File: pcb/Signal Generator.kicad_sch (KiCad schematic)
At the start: 3 parts, among them J2 AudioJack3, J3 Conn_02x02_Odd_Even, J4 Screw_Terminal_01x04

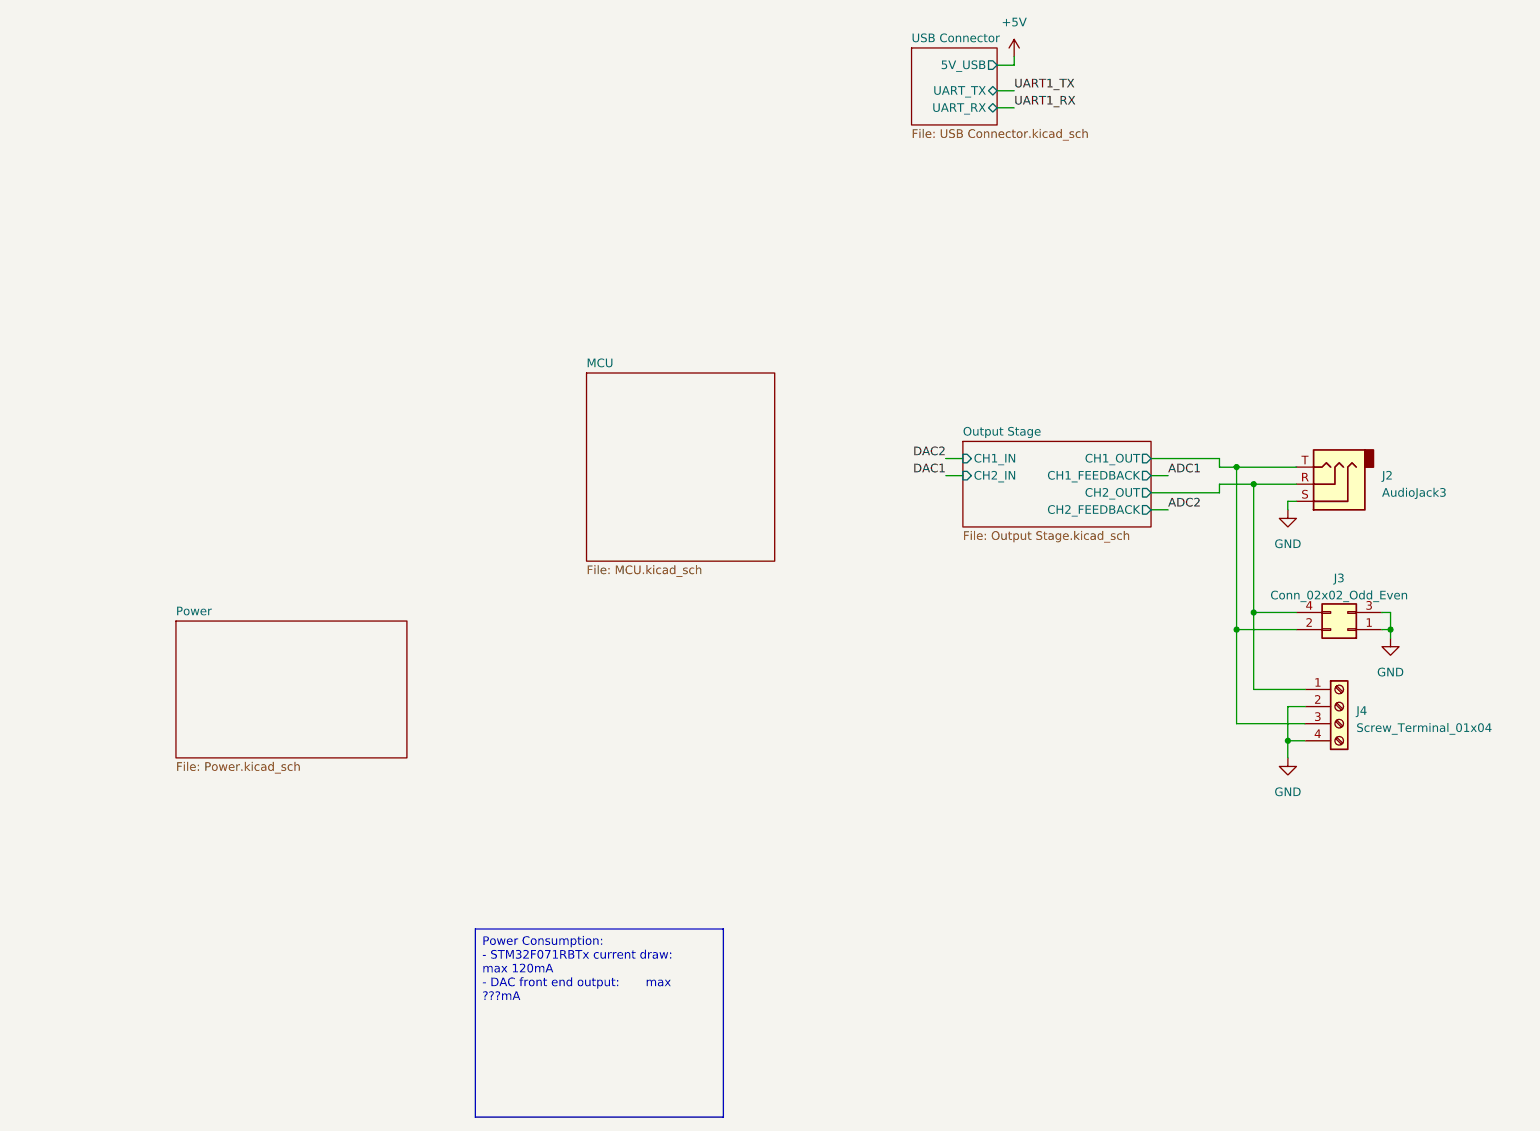
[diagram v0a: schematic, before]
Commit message: Completed schematic oranization and components connection
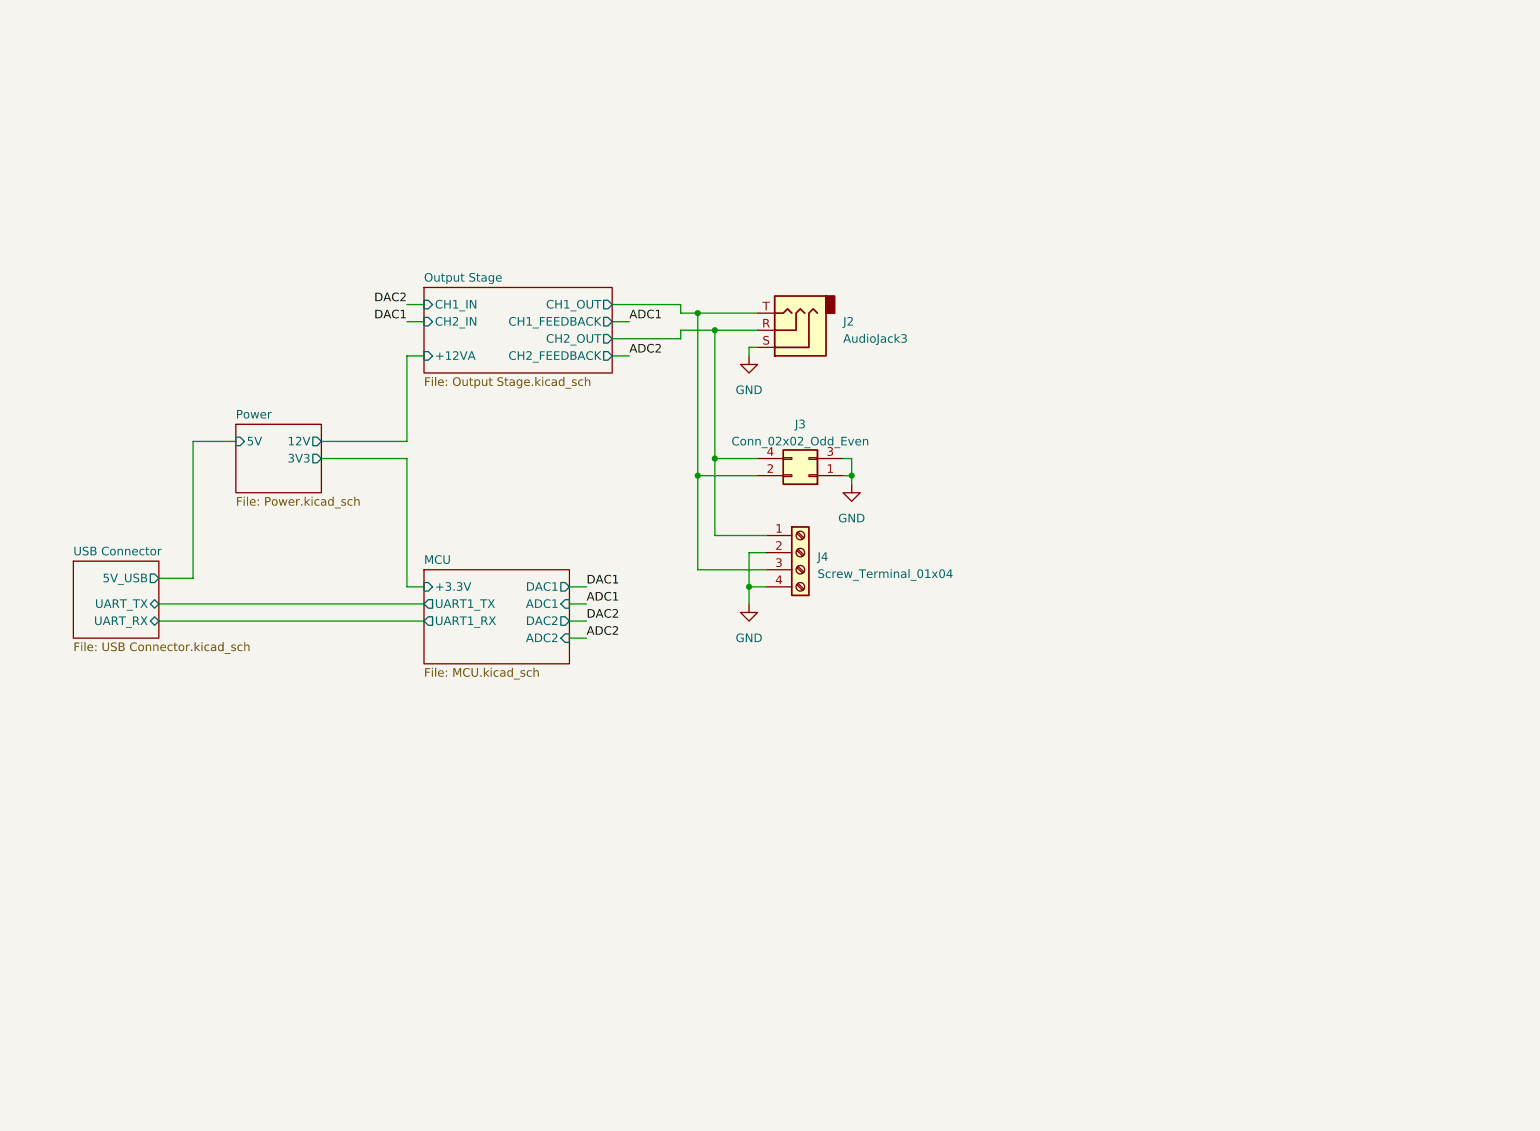
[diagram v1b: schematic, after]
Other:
- sheet MCU ports: added +3.3V, ADC1, ADC2, DAC1, DAC2, UART1_RX, UART1_TX; removed none
- sheet Output Stage ports: added +12VA; removed none
- sheet Power ports: added 12V, 3V3, 5V; removed none
- moved on the sheet: J2, J3, J4

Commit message: Added micro SD and RGB led to schematic. Also added components part numbers
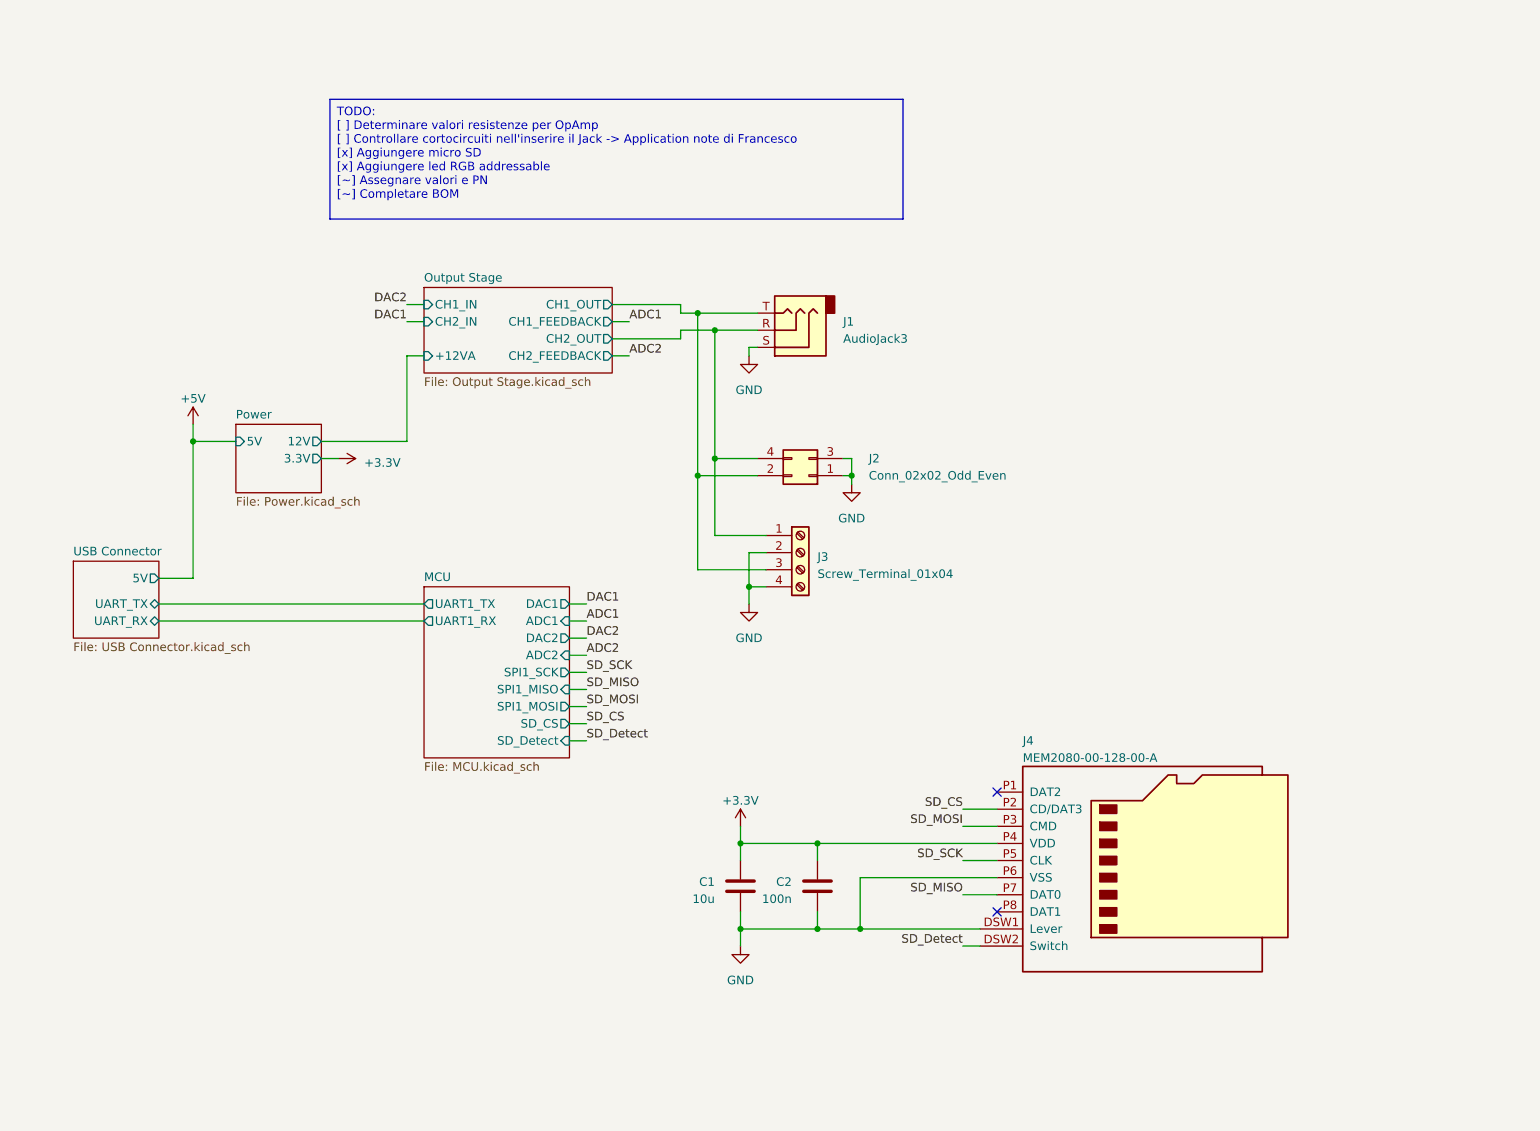
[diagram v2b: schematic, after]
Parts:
- added C1: 10u, Capacitor_SMD:C_0603_1608Metric, symbol Device:C
- added C2: 100n, Capacitor_SMD:C_0603_1608Metric, symbol Device:C
- added J4: MEM2080-00-128-00-A, Signal Generator Components:MEM2080-00-128-00-A, symbol Signal Generator Components:MEM2080-00-128-00-A
- J1: renamed from J2; PN (none) -> SJ-3523-SMT-TR
- J2: renamed from J3; PN (none) -> 10129382-904001BLF
- J3: renamed from J4; PN (none) -> 1725672
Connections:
- net GND: now also C1.2, C2.2, J4.DSW1 (Lever), J4.P6 (VSS)
- new net +3.3V: C1.1, C2.1, J4.P4 (VDD)
- new net SD_CS: J4.P2 (CD/DAT3)
- new net SD_Detect: J4.DSW2 (Switch)
- new net SD_MISO: J4.P7 (DAT0)
- new net SD_MOSI: J4.P3 (CMD)
- new net SD_SCK: J4.P5 (CLK)
- no-connect marks 0 -> 2
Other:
- sheet MCU ports: added SD_CS, SD_Detect, SPI1_MISO, SPI1_MOSI, SPI1_SCK; removed +3.3V
- sheet Power ports: added 3.3V; removed 3V3
- sheet USB Connector ports: added 5V; removed 5V_USB

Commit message: Completed schematic and tried some simulations
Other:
- moved on the sheet: J1, J2, J3

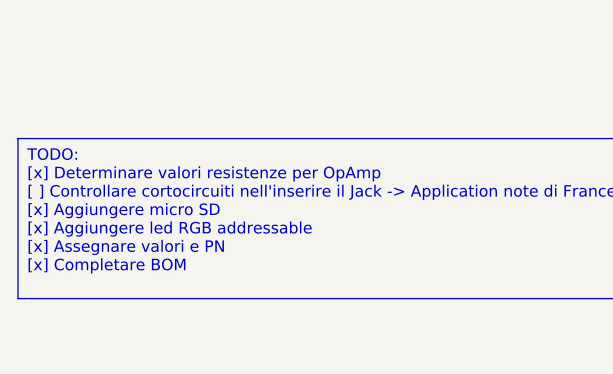
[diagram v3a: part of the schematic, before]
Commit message: Added ST-Link connector to schematic
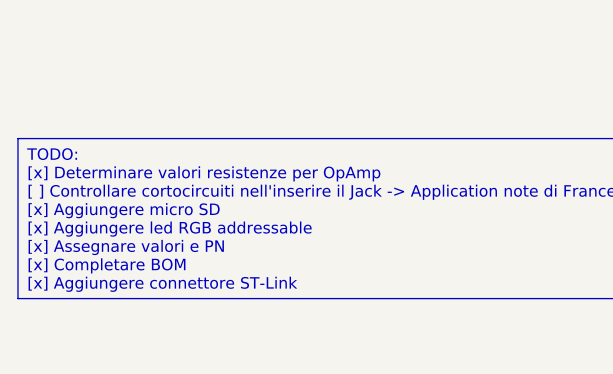
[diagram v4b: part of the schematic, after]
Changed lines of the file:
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@@
     (stroke (width 0) (type default))
   )
-  (text_box "TODO:\n [x] Determinare valori resistenze per OpAmp\n [ ] Controllare cortocircuiti nell'inserire il Jack -> Application note di Francesco\n [x] Aggiungere micro SD\n [x] Aggiungere led RGB addressable\n [x] Assegnare valori e PN\n [x] Completare BOM"
+  (text_box "TODO:\n [x] Determinare valori resistenze per OpAmp\n [ ] Controllare cortocircuiti nell'inserire il Jack -> Application note di Francesco\n [x] Aggiungere micro SD\n [x] Aggiungere led RGB addressable\n [x] Assegnare valori e PN\n [x] Completare BOM\n [x] Aggiungere connettore ST-Link"
     (at 63.5 149.86 0) (size 85.09 17.78)
     (stroke (width 0) (type default))

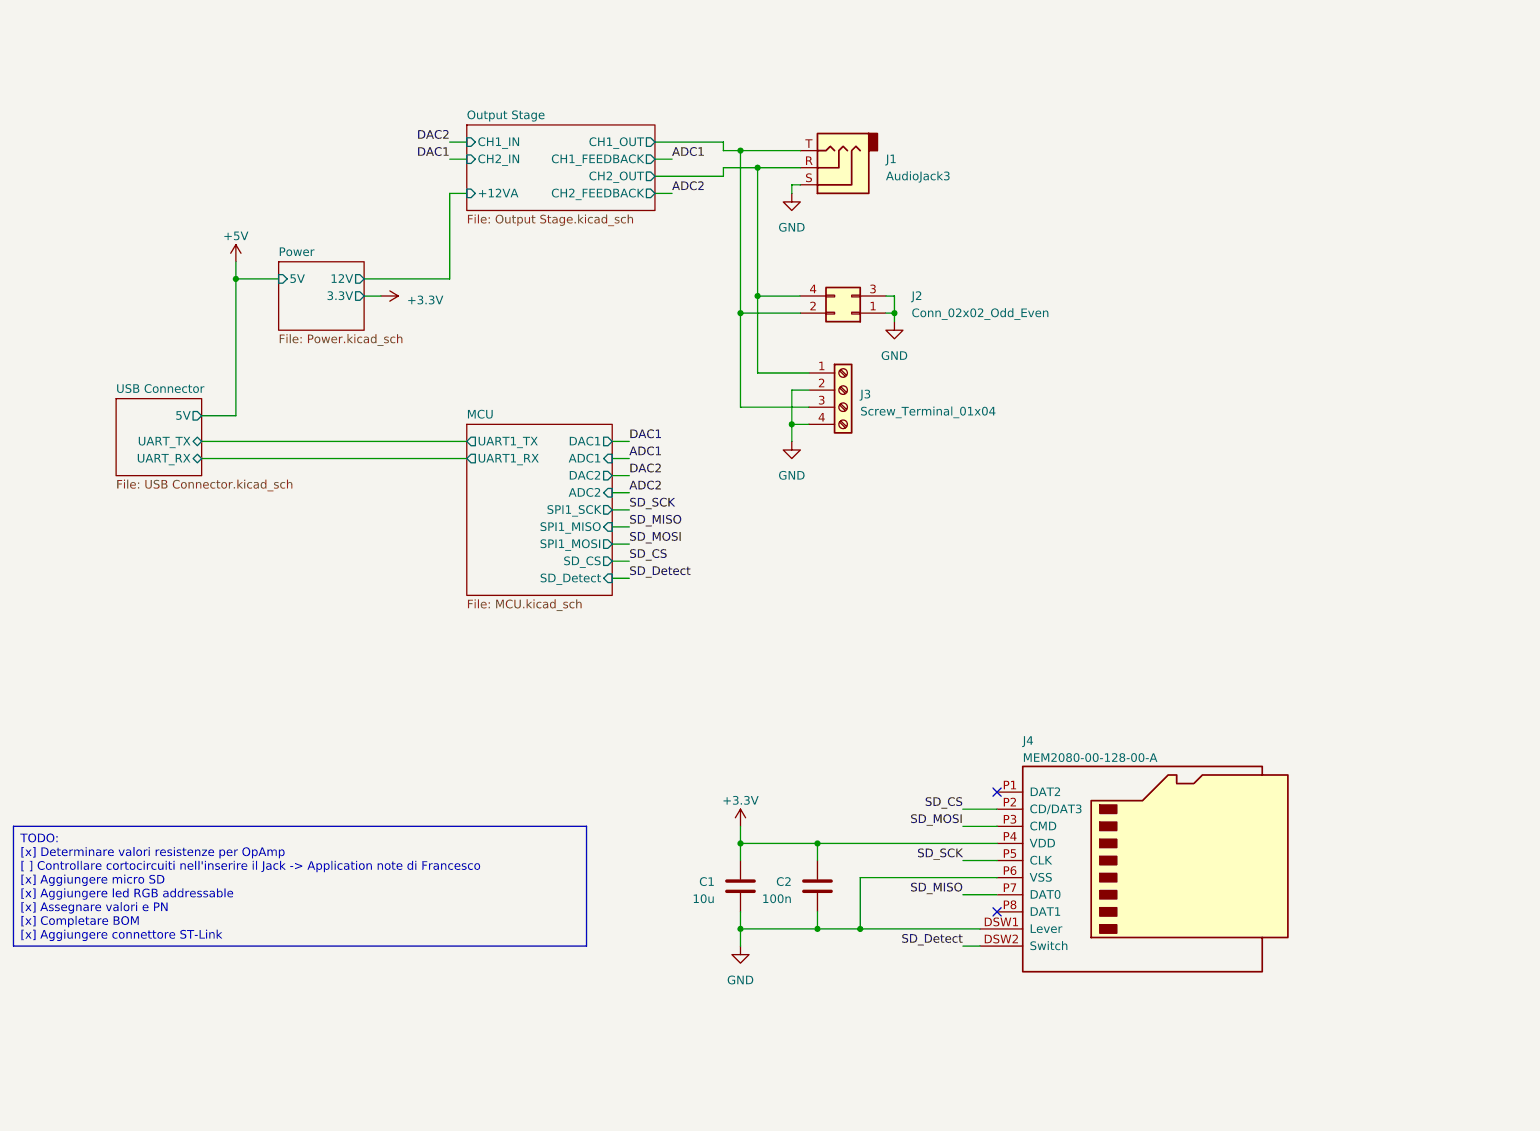
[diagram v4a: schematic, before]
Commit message: Added blocking capacitor to headphones jack
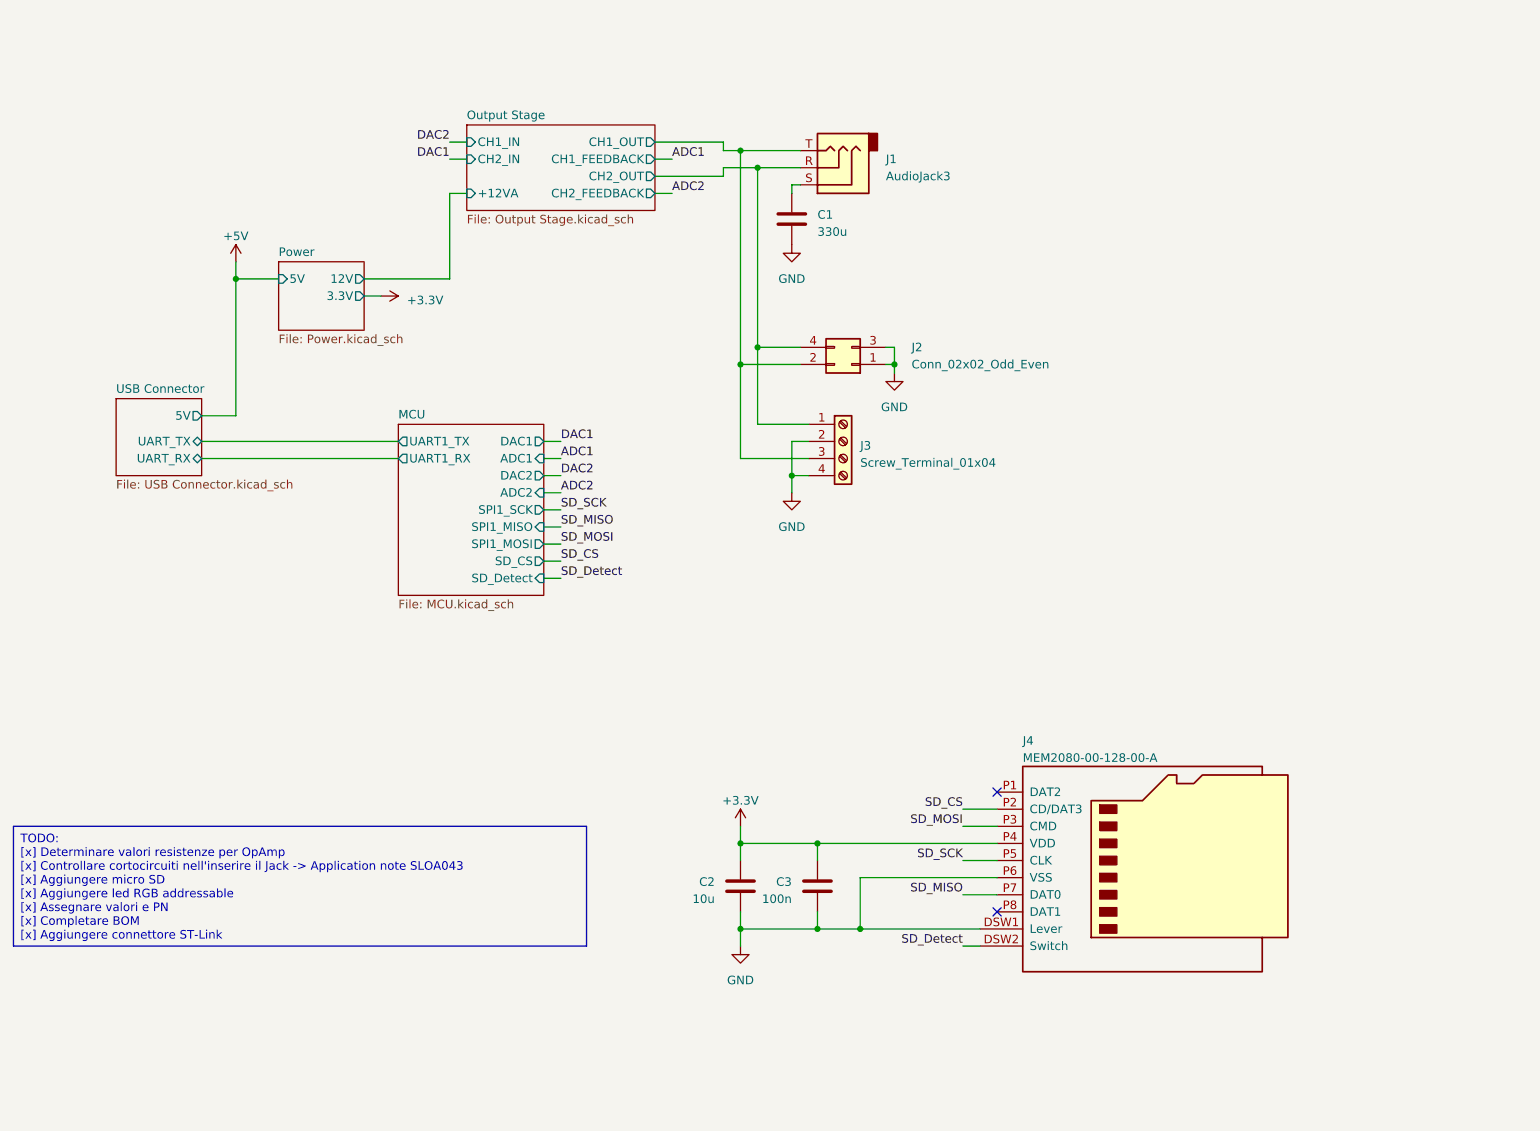
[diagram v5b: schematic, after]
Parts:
- added C1: 330u, symbol Device:C
- renumbered C1 to C2, C2 to C3
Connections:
- net GND: now also C1.2; no longer J1.S
- new net: C1.1, J1.S
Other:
- moved on the sheet: J2, J3

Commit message: Updated some footprints
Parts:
- C1: footprint (none) -> Signal Generator Components:WCAP-PSHP
- J1: footprint Connector_Audio:Jack_3.5mm_CUI_SJ-3523-SMT_Horizontal -> Signal Generator Components:SJ-3523-SMT-TR-1
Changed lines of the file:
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@@
       (effects (font (size 1.27 1.27)) (justify left))
     )
-    (property "Footprint" "" (at 180.0352 63.5 0)
+    (property "Footprint" "Signal Generator Components:WCAP-PSHP" (at 180.0352 63.5 0)
       (effects (font (size 1.27 1.27)) hide)
     )
@@
       (effects (font (size 1.27 1.27)) (justify right))
     )
-    (property "Footprint" "Connector_Audio:Jack_3.5mm_CUI_SJ-3523-SMT_Horizontal" (at 185.42 52.07 0)
+    (property "Footprint" "Signal Generator Components:SJ-3523-SMT-TR-1" (at 185.42 52.07 0)
       (effects (font (size 1.27 1.27)) hide)
     )
